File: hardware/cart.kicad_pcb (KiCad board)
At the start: 2 copper layers, 83.7 x 42 mm, 30 parts, among them J2 debug-power, J3 debug-flash, P1 edge connector, U1 74LVC138, U2 1.5A @ 3.3V, U3 74LVC8T245, U4 74LVC8T245, U5 74LVC8T245, U6 S29AL016J55TFIR20, U7 74LVC8T245, U8 74LVC8T245

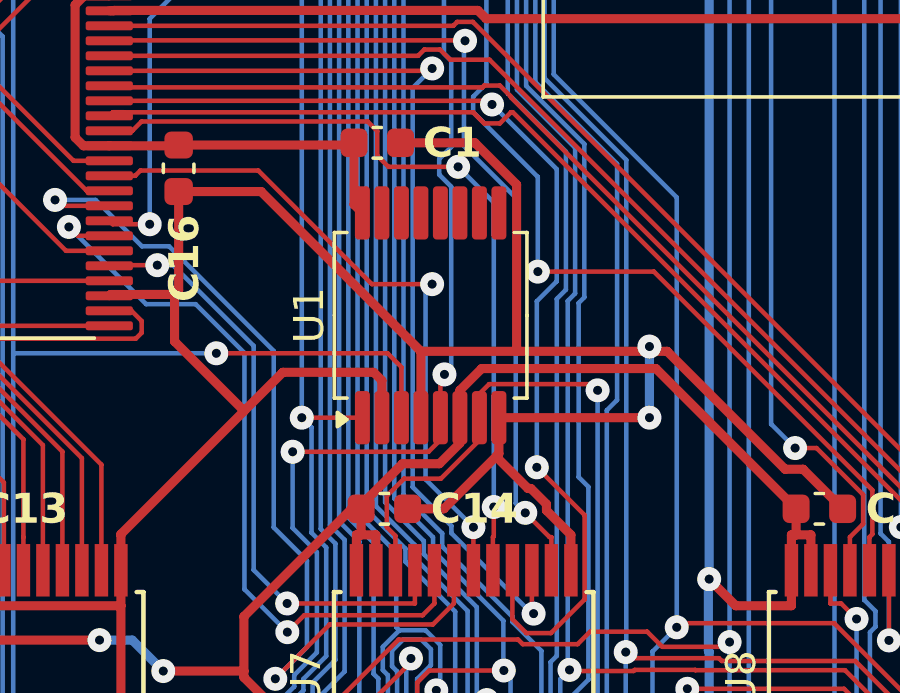
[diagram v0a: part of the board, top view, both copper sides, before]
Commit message: Fix footprint of new address decoder on cart board
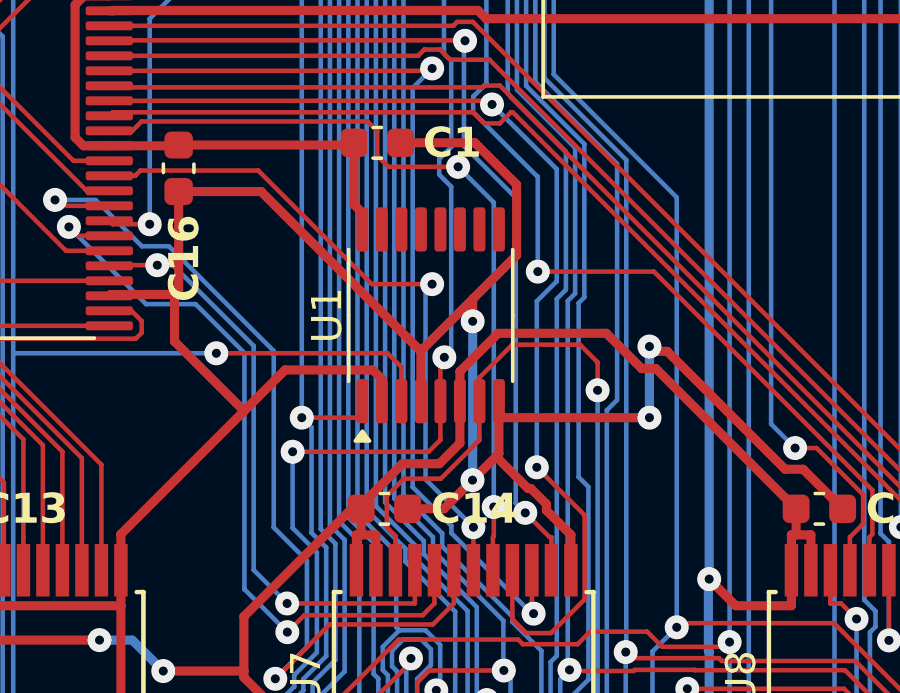
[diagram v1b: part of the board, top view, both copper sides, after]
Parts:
- U1: footprint Package_SO:SSOP-16_5.3x6.2mm_P0.65mm -> Package_SO:TSSOP-16_4.4x5mm_P0.65mm
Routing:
- net /~{FLASH_CE}: track 73.8 -> 76.3 mm
- net +3.3V: track 286.8 -> 288.5 mm
- net GND: track 436.0 -> 434.8 mm, vias 6 -> 8
- net /~{SEGA_AS}: track 77.2 -> 76.6 mm

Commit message: Bump cart date
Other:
- board text added: "2024-06-22"
- board text removed: "2024-06-21"
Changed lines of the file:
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@@
 		)
 	)
-	(gr_text "2024-06-21"
+	(gr_text "2024-06-22"
 		(at 17.5 32 90)
 		(layer "F.SilkS")
@@
 			)
 		)
-		(render_cache "2024-06-21" 90
+		(render_cache "2024-06-22" 90
 			(polygon
 				(pts
@@
 			(polygon
 				(pts
-					(xy 16.329162 24.563293) (xy 16.329162 24.307327) (xy 18.085757 24.307327) (xy 18.085757 23.800767)
-					(xy 18.33 23.800767) (xy 18.33 25.08353) (xy 18.085757 25.08353) (xy 18.085757 24.574528) (xy 16.703831 24.574528)
-					(xy 17.054075 24.912072) (xy 16.843538 25.049825)
+					(xy 16.329162 24.84173) (xy 16.329162 24.023028) (xy 16.68136 23.797836) (xy 16.969567 23.797836)
+					(xy 18.020788 24.81926) (xy 18.085757 24.81926) (xy 18.085757 23.797836) (xy 18.33 23.797836) (xy 18.33 25.081088)
+					(xy 17.947515 25.081088) (xy 16.832791 24.000558) (xy 16.573405 24.166643) (xy 16.573405 24.740613)
+					(xy 16.793224 24.951639) (xy 16.593921 25.086461)
 				)
 			)

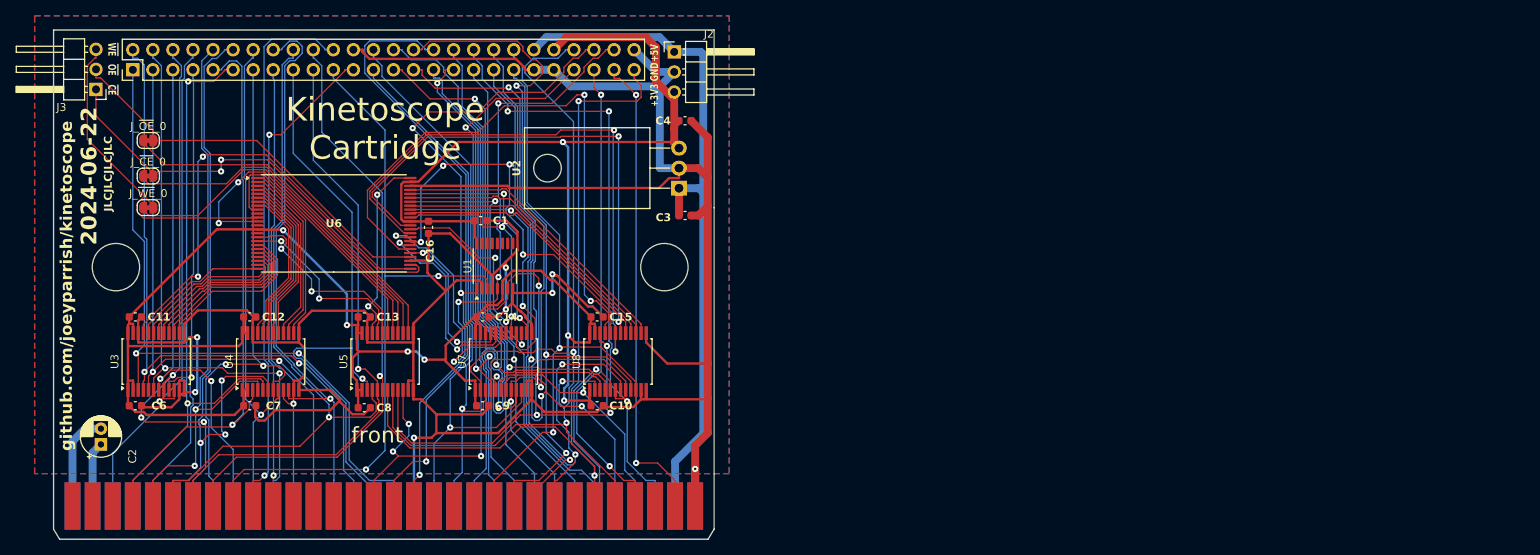
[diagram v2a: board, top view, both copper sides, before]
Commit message: Fix cartridge board mistakes from v0.0.2
After getting the v0.0.2 cart board assembled, I found and fixed
several issues:
 - Fix address decoder output (Y0, not Y7)
 - Fix level-shifter direction for data (was backwards before)
 - Fix debug pad access to signals (level-shifters should use the
   internal signal, not the external one)
 - Avoid traces too close to the debug pads, since they can be cut
   accidentally

Also:
 - Add additional debug pad for both raw and level-shifted signals
 - Add debug pad and pin header for measuring current consumption
 - Replace bulk capacitor with SMD version
 - Remove pin headers that I didn't find all that useful in the last
   revision
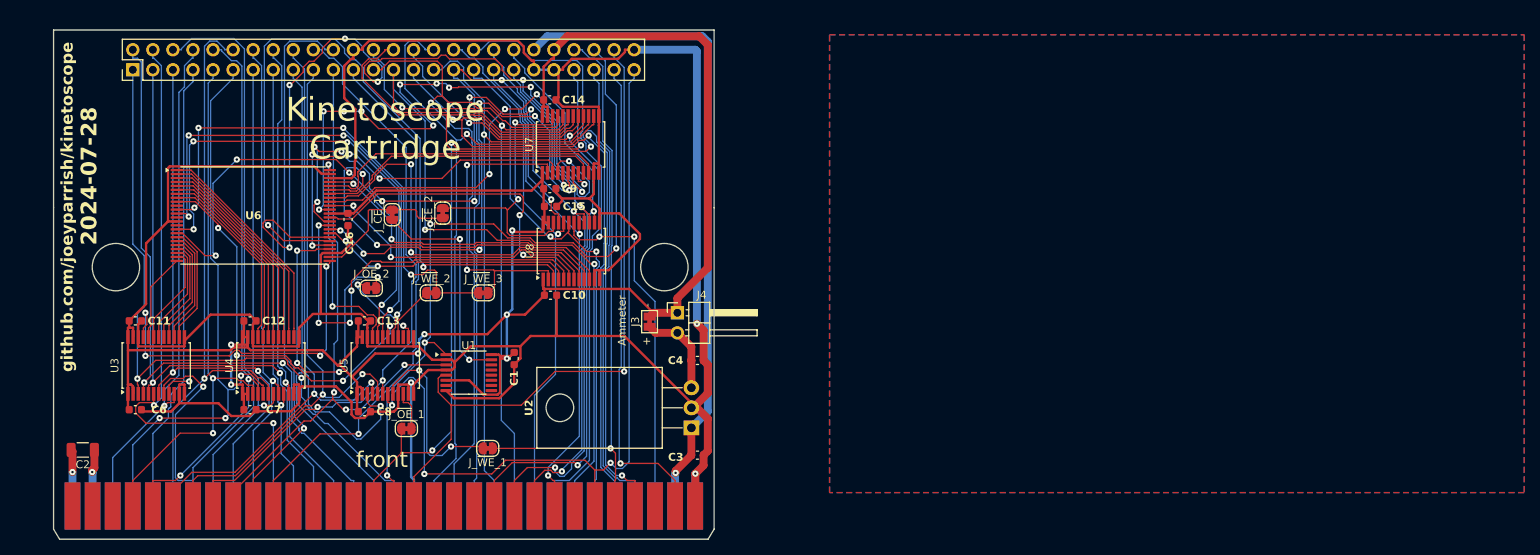
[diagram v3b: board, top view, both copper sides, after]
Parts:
- removed J2: debug-power, Connector_PinHeader_2.54mm:PinHeader_1x03_P2.54mm_Horizontal
- removed J_~{CE}_0, J_~{OE}_0, J_~{WE}_0: jumper-bridged, Jumper:SolderJumper-2_P1.3mm_Bridged_RoundedPad1.0x1.5mm
- added J4: debug-snoop, Connector_PinHeader_2.54mm:PinHeader_1x02_P2.54mm_Horizontal, F.Cu at (92.0, 49.3)
- added J_~{CE}_1: jumper-bridged, Jumper:SolderJumper-2_P1.3mm_Bridged_RoundedPad1.0x1.5mm, F.Cu at (55.9, 36.9)
- added J_~{CE}_2: jumper-bridged, Jumper:SolderJumper-2_P1.3mm_Bridged_RoundedPad1.0x1.5mm, F.Cu at (62.3, 36.7)
- added J_~{OE}_1: jumper-bridged, Jumper:SolderJumper-2_P1.3mm_Bridged_RoundedPad1.0x1.5mm, F.Cu at (57.7, 64.0)
- added J_~{OE}_2: jumper-bridged, Jumper:SolderJumper-2_P1.3mm_Bridged_RoundedPad1.0x1.5mm, F.Cu at (53.2, 46.2)
- added J_~{WE}_1: jumper-bridged, Jumper:SolderJumper-2_P1.3mm_Bridged_RoundedPad1.0x1.5mm, F.Cu at (68.0, 66.5)
- added J_~{WE}_2: jumper-bridged, Jumper:SolderJumper-2_P1.3mm_Bridged_RoundedPad1.0x1.5mm, F.Cu at (60.9, 46.8)
- added J_~{WE}_3: jumper-bridged, Jumper:SolderJumper-2_P1.3mm_Bridged_RoundedPad1.0x1.5mm, F.Cu at (67.5, 46.8)
- C2: footprint Capacitor_THT:CP_Radial_D5.0mm_P2.00mm -> Capacitor_SMD:C_1206_3216Metric
- J3: value debug-flash -> jumper-bridged; footprint Connector_PinHeader_2.54mm:PinHeader_1x03_P2.54mm_Horizontal -> Jumper:SolderJumper-2_P1.3mm_Bridged_Pad1.0x1.5mm
- moved J3 76.0 mm to (88.5, 50.5), turned to 90 degrees
- moved C3 30.4 mm to (94.6, 67.4)
- moved C4 30.4 mm to (94.6, 55.4)
- moved U2 30.4 mm to (93.8, 63.9)
- moved C14 28.8 mm to (75.9, 22.4)
- moved C9 28.8 mm to (75.9, 33.6)
- moved U7 28.8 mm to (78.5, 28.0)
- moved C1 18.0 mm to (71.3, 55.1), turned to -90 degrees
- moved C10 15.2 mm to (76.0, 47.1)
- moved C15 15.2 mm to (76.0, 35.9)
- moved U8 15.2 mm to (78.6, 41.5)
- moved U1 13.9 mm to (65.6, 56.9), turned to 0 degrees
- moved C16 10.2 mm to (50.3, 37.5)
- moved U6 10.2 mm to (38.3, 37.0)
- moved C2 2.40 mm to (16.7, 66.7), turned to 180 degrees
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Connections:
- C4 pad 1: +3.3V -> Net-(J3-A)
- J3 pad 1: /flash-internal/~{CE_3V} -> Net-(J3-A)
- J3 pad 2: /flash-internal/~{OE_3V} -> +3.3V
- U1 pad 15: unconnected-(U1-~{Y0}-Pad15) -> /~{FLASH_CE}
- U1 pad 7: /~{FLASH_CE} -> unconnected-(U1-~{Y7}-Pad7)
- U2 pad 3: +3.3V -> Net-(J3-A)
- U5 pad 10: /~{SEGA_OE} -> /flash-internal/~{OE_INT}
- U5 pad 14: Net-(J_~{OE}_0-A) -> /flash-internal/~{OE_3V}
- U5 pad 15: Net-(J_~{CE}_0-A) -> unconnected-(U5-B7-Pad15)
- U5 pad 16: Net-(J_~{WE}_0-A) -> /flash-internal/~{WE_3V}
- U5 pad 8: /~{SEGA_WE_LB} -> /flash-internal/~{WE_INT}
- U5 pad 9: /~{FLASH_CE} -> GND
- U6 pad 11: /flash-internal/~{WE_3V} -> /flash-internal/~{WE_3V_INT}
- U6 pad 26: /flash-internal/~{CE_3V} -> /flash-internal/~{CE_3V_INT}
- U6 pad 28: /flash-internal/~{OE_3V} -> /flash-internal/~{OE_3V_INT}
- U7 pad 10: /SEGA_D7 -> /flash-internal/D7_3V
- U7 pad 14: /flash-internal/D7_3V -> /SEGA_D7
- U7 pad 15: /flash-internal/D6_3V -> /SEGA_D6
- U7 pad 16: /flash-internal/D5_3V -> /SEGA_D5
- U7 pad 17: /flash-internal/D4_3V -> /SEGA_D4
- U7 pad 18: /flash-internal/D3_3V -> /SEGA_D3
- U7 pad 19: /flash-internal/D2_3V -> /SEGA_D2
- U7 pad 2: /~{SEGA_WE_LB} -> /flash-internal/DATA_DIR_INT
- U7 pad 20: /flash-internal/D1_3V -> /SEGA_D1
- U7 pad 21: /flash-internal/D0_3V -> /SEGA_D0
- U7 pad 22: /~{FLASH_CE} -> /flash-internal/~{DATA_OE_INT}
- U7 pad 3: /SEGA_D0 -> /flash-internal/D0_3V
- U7 pad 4: /SEGA_D1 -> /flash-internal/D1_3V
- U7 pad 5: /SEGA_D2 -> /flash-internal/D2_3V
- U7 pad 6: /SEGA_D3 -> /flash-internal/D3_3V
- U7 pad 7: /SEGA_D4 -> /flash-internal/D4_3V
- U7 pad 8: /SEGA_D5 -> /flash-internal/D5_3V
- U7 pad 9: /SEGA_D6 -> /flash-internal/D6_3V
- U8 pad 10: /SEGA_D15 -> /flash-internal/D15_3V
- U8 pad 14: /flash-internal/D15_3V -> /SEGA_D15
- U8 pad 15: /flash-internal/D14_3V -> /SEGA_D14
- U8 pad 16: /flash-internal/D13_3V -> /SEGA_D13
- U8 pad 17: /flash-internal/D12_3V -> /SEGA_D12
- U8 pad 18: /flash-internal/D11_3V -> /SEGA_D11
- U8 pad 19: /flash-internal/D10_3V -> /SEGA_D10
- U8 pad 2: /~{SEGA_WE_LB} -> /flash-internal/DATA_DIR_INT
- U8 pad 20: /flash-internal/D9_3V -> /SEGA_D9
- U8 pad 21: /flash-internal/D8_3V -> /SEGA_D8
- U8 pad 22: /~{FLASH_CE} -> /flash-internal/~{DATA_OE_INT}
- U8 pad 3: /SEGA_D8 -> /flash-internal/D8_3V
- U8 pad 4: /SEGA_D9 -> /flash-internal/D9_3V
- U8 pad 5: /SEGA_D10 -> /flash-internal/D10_3V
- U8 pad 6: /SEGA_D11 -> /flash-internal/D11_3V
- U8 pad 7: /SEGA_D12 -> /flash-internal/D12_3V
- U8 pad 8: /SEGA_D13 -> /flash-internal/D13_3V
- U8 pad 9: /SEGA_D14 -> /flash-internal/D14_3V
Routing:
- net /flash-internal/D1_3V: track 25.4 -> 106.0 mm, vias 2 -> 6
- net /flash-internal/~{WE_3V_INT}: track 0.00 -> 64.6 mm, vias 0 -> 4
- net /flash-internal/~{CE_3V}: track 56.9 -> 0.00 mm, vias 2 -> 0
- net /flash-internal/D3_3V: track 22.7 -> 72.9 mm, vias 2 -> 8
- net /~{FLASH_CE}: track 76.3 -> 28.2 mm, vias 4 -> 2
- net /~{SEGA_WE_LB}: track 124.1 -> 76.1 mm, vias 3 -> 1
- net Net-(J_~{WE}_0-A): track 46.2 -> 0.00 mm
- net Net-(J_~{OE}_0-A): track 45.9 -> 0.00 mm
- net GND: track 434.8 -> 389.3 mm, vias 8 -> 3
- net Net-(J_~{CE}_0-A): track 45.3 -> 0.00 mm
- net /flash-internal/D4_3V: track 26.8 -> 71.7 mm, vias 2 -> 10
- net /flash-internal/~{OE_3V_INT}: track 0.00 -> 41.2 mm, vias 0 -> 4
- net /flash-internal/~{OE_3V}: track 51.0 -> 11.3 mm, vias 0 -> 2
- net /flash-internal/DATA_DIR_INT: track 0.00 -> 39.2 mm, vias 0 -> 2
- net /flash-internal/A18_3V: track 25.3 -> 61.7 mm, vias 2 -> 4
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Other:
- board text added: "+"
- board text added: "-"
- board text added: "2024-07-28"
- board text added: "Ammeter"
- board text removed: "+3V3"
- board text removed: "+5V"
- board text removed: "2024-06-22"
- board text removed: "GND"
- board text removed: "JLCJLCJLCJLC"
- board text removed: "~{CE}"
- board text removed: "~{OE}"
- board text removed: "~{WE}"

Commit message: Fix missing ground plane in cart PCB
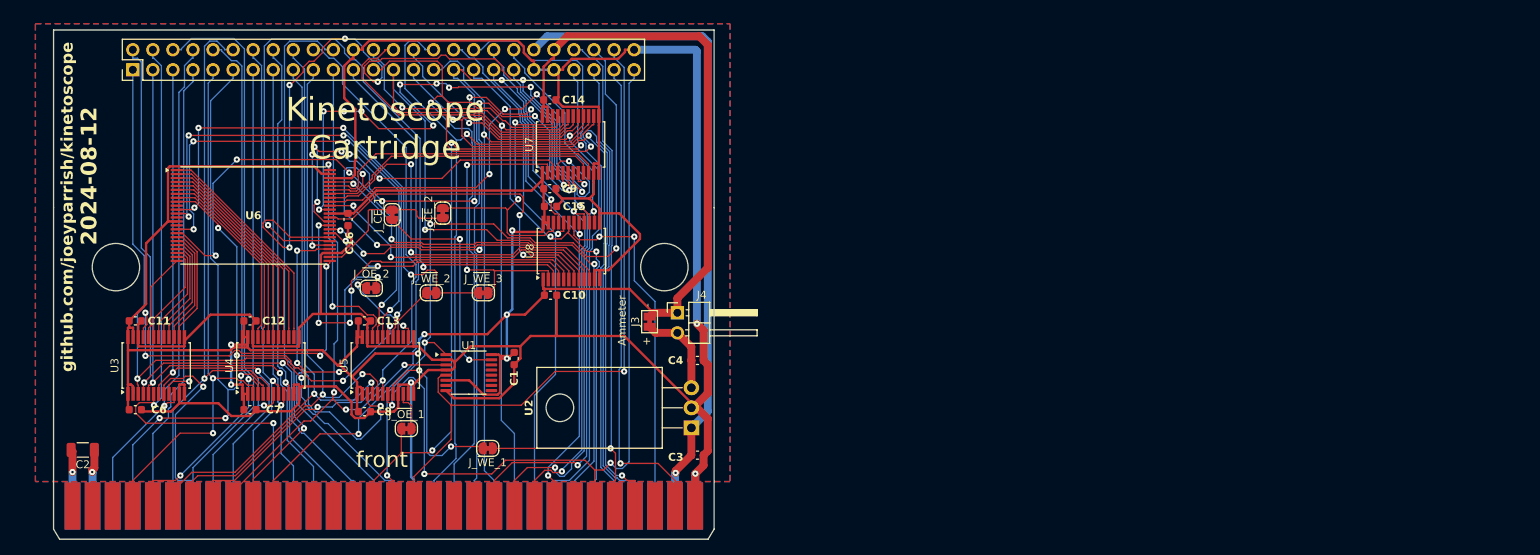
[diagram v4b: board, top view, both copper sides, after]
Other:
- board text added: "2024-08-12"
- board text removed: "2024-07-28"
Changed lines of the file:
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@@
 		)
 	)
-	(gr_text "2024-07-28"
+	(gr_text "2024-08-12"
 		(at 17.5 32 90)
 		(layer "F.SilkS")
@@
 			)
 		)
-		(render_cache "2024-07-28" 90
+		(render_cache "2024-08-12" 90
 			(polygon
 				(pts
@@
 			(polygon
 				(pts
-					(xy 16.329162 30.118841) (xy 16.329162 28.836077) (xy 16.741444 28.836077) (xy 17.547934 29.629378)
-					(xy 18.33 29.629378) (xy 18.33 29.89658) (xy 17.472219 29.89658) (xy 16.665729 29.103279) (xy 16.573405 29.103279)
-					(xy 16.573405 30.118841)
+					(xy 17.295875 29.08374) (xy 17.667613 28.836077) (xy 17.978778 28.836077) (xy 18.33 29.167759)
+					(xy 18.33 29.879971) (xy 17.976336 30.118841) (xy 17.628534 30.118841) (xy 17.371591 29.862874)
+					(xy 17.371591 29.891207) (xy 17.035024 30.118841) (xy 16.785896 30.118841) (xy 16.329162 29.685554)
+					(xy 16.329162 29.178994) (xy 16.573405 29.178994) (xy 16.573405 29.581507) (xy 16.85575 29.85457)
+					(xy 16.995945 29.85457) (xy 17.142002 29.755896) (xy 17.142002 29.317236) (xy 17.386245 29.317236)
+					(xy 17.386245 29.556105) (xy 17.701318 29.85457) (xy 17.936769 29.85457) (xy 18.085757 29.752965)
+					(xy 18.085757 29.280599) (xy 17.911856 29.103279) (xy 17.706692 29.103279) (xy 17.386245 29.317236)
+					(xy 17.142002 29.317236) (xy 17.142002 29.280599) (xy 16.968101 29.103279) (xy 16.690642 29.103279)
+					(xy 16.573405 29.178994) (xy 16.329162 29.178994) (xy 16.329162 29.044172) (xy 16.651563 28.836077)
+					(xy 17.035024 28.836077)
 				)
 			)
@@
 			(polygon
 				(pts
-					(xy 16.329162 26.520167) (xy 16.329162 25.701465) (xy 16.68136 25.476273) (xy 16.969567 25.476273)
-					(xy 18.020788 26.497696) (xy 18.085757 26.497696) (xy 18.085757 25.476273) (xy 18.33 25.476273)
-					(xy 18.33 26.759525) (xy 17.947515 26.759525) (xy 16.832791 25.678994) (xy 16.573405 25.84508)
-					(xy 16.573405 26.41905) (xy 16.793224 26.630076) (xy 16.593921 26.764898)
+					(xy 16.329162 26.24173) (xy 16.329162 25.985763) (xy 18.085757 25.985763) (xy 18.085757 25.479204)
+					(xy 18.33 25.479204) (xy 18.33 26.761967) (xy 18.085757 26.761967) (xy 18.085757 26.252965) (xy 16.703831 26.252965)
+					(xy 17.054075 26.590509) (xy 16.843538 26.728262)
 				)
 			)
 			(polygon
 				(pts
-					(xy 17.295875 24.048429) (xy 17.667613 23.800767) (xy 17.978778 23.800767) (xy 18.33 24.132449)
-					(xy 18.33 24.844661) (xy 17.976336 25.08353) (xy 17.628534 25.08353) (xy 17.371591 24.827564) (xy 17.371591 24.855896)
-					(xy 17.035024 25.08353) (xy 16.785896 25.08353) (xy 16.329162 24.650244) (xy 16.329162 24.143684)
-					(xy 16.573405 24.143684) (xy 16.573405 24.546196) (xy 16.85575 24.81926) (xy 16.995945 24.81926)
-					(xy 17.142002 24.720585) (xy 17.142002 24.281925) (xy 17.386245 24.281925) (xy 17.386245 24.520795)
-					(xy 17.701318 24.81926) (xy 17.936769 24.81926) (xy 18.085757 24.717655) (xy 18.085757 24.245289)
-					(xy 17.911856 24.067969) (xy 17.706692 24.067969) (xy 17.386245 24.281925) (xy 17.142002 24.281925)
-					(xy 17.142002 24.245289) (xy 16.968101 24.067969) (xy 16.690642 24.067969) (xy 16.573405 24.143684)
-					(xy 16.329162 24.143684) (xy 16.329162 24.008862) (xy 16.651563 23.800767) (xy 17.035024 23.800767)
+					(xy 16.329162 24.84173) (xy 16.329162 24.023028) (xy 16.68136 23.797836) (xy 16.969567 23.797836)
+					(xy 18.020788 24.81926) (xy 18.085757 24.81926) (xy 18.085757 23.797836) (xy 18.33 23.797836) (xy 18.33 25.081088)
+					(xy 17.947515 25.081088) (xy 16.832791 24.000558) (xy 16.573405 24.166643) (xy 16.573405 24.740613)
+					(xy 16.793224 24.951639) (xy 16.593921 25.086461)
 				)
 			)
@@
 		(polygon
 			(pts
-				(xy 111.3 14.1) (xy 199.3 14.1) (xy 199.3 72.1) (xy 111.3 72.1)
+				(xy 10.7 12.7) (xy 98.7 12.7) (xy 98.7 70.7) (xy 10.7 70.7)
 			)
 		)
